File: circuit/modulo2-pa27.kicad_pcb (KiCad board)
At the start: 2 copper layers, 105 x 47 mm, 48 parts, among them J1 CONN_01X02, J3 CONN_01X04, J4 JACK_MONO, J5 HOLE, J7 HOLE, SW1 bright, U1 OPA2134, U2 OPA2134, U3 TLE2426, U4 PWR_CONN

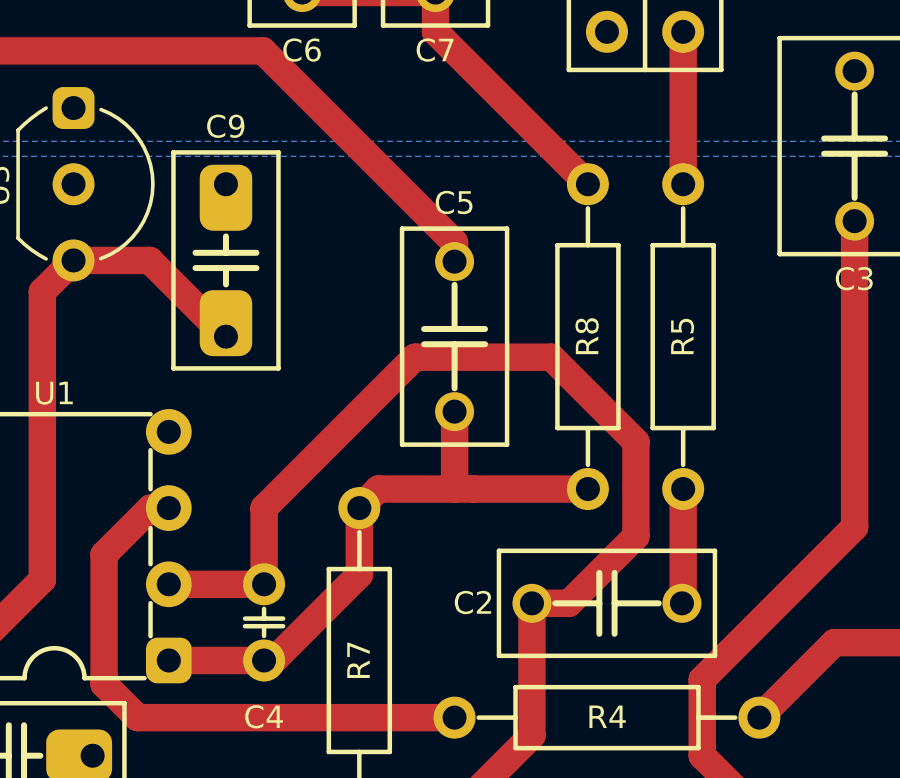
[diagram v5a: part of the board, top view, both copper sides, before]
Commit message: fixed mistakes from assembly; added bootloader; firmware changed for PCB
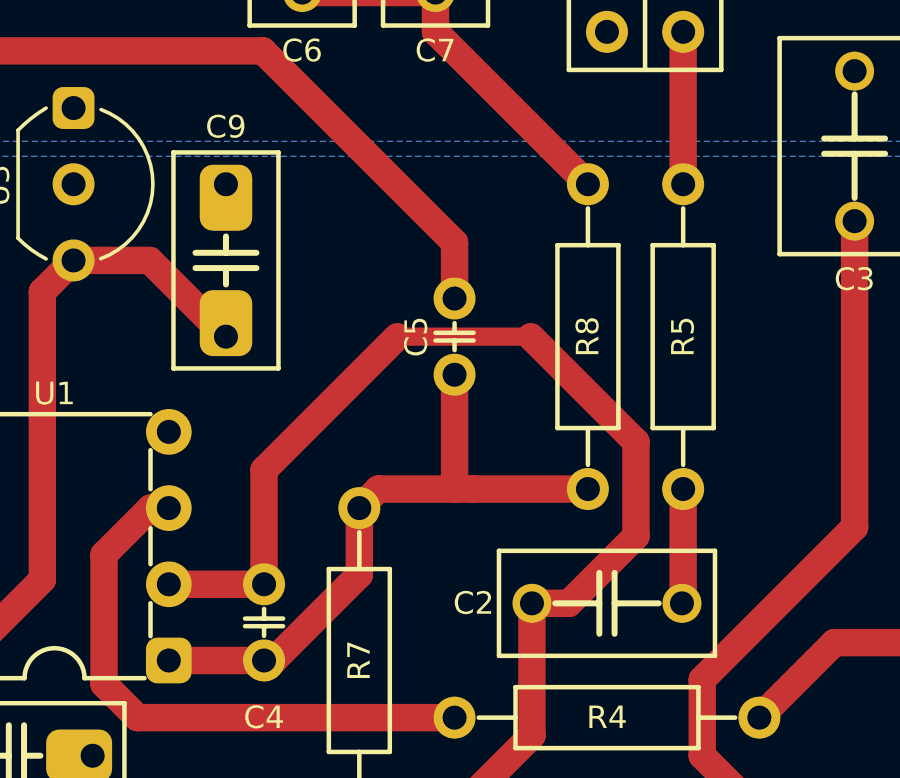
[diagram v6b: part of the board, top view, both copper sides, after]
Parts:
- C1: value 47nF -> 150nF
- C5: footprint myAmp:C_FILM_L7.2mm_W3.5mm_P5.00mm -> myAmp:C_2.5MM
- R15: value 10k -> 4k7
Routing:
- net Net-(C2-Pad2): track 40.1 -> 41.4 mm
- net Net-(C4-Pad2): track 20.2 -> 21.4 mm
- net /TRB: track 33.5 -> 34.7 mm
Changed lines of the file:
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@@
     )
   )
-  (footprint "myAmp:C_FILM_L7.2mm_W3.5mm_P5.00mm" (layer "F.Cu")
+  (footprint "myAmp:C_2.5MM" (layer "F.Cu")
     (at 107.95 72.39 90)
     (property "Sheetfile" "modulo2-pa27.kicad_sch")
     (property "Sheetname" "")
     (attr through_hole)
-    (fp_text reference "C5" (at 4.445 0) (layer "F.SilkS")
-      (effects (font (size 0.75 0.75) (thickness 0.15)))
-    )
-    (fp_text value "250pF" (at -1.016 -0.254 90) (layer "F.Fab") hide
-      (effects (font (size 0.0254 0.0254) (thickness 0.001)))
-    )
-    (fp_line (start -0.254 -1.016) (end -0.254 1.016) (layer "F.SilkS") (width 0.2))
-    (fp_line (start -3.6 -1.75) (end -3.6 1.75) (layer "F.SilkS") (width 0.15))
-    (fp_line (start -3.6 1.75) (end 3.6 1.75) (layer "F.SilkS") (width 0.15))
-    (fp_line (start 0.254 0) (end 1.725 0) (layer "F.SilkS") (width 0.2))
-    (fp_line (start 0.254 -1.016) (end 0.254 1.016) (layer "F.SilkS") (width 0.2))
-    (fp_line (start 3.6 -1.75) (end -3.6 -1.75) (layer "F.SilkS") (width 0.15))
-    (fp_line (start -0.254 0) (end -1.725 0) (layer "F.SilkS") (width 0.2))
-    (fp_line (start 3.6 1.75) (end 3.6 -1.75) (layer "F.SilkS") (width 0.15))
-    (pad "1" thru_hole circle (at -2.5 0 90) (size 1.3 1.3) (drill 0.8) (layers *.Cu *.Mask)
+    (fp_text reference "C5" (at 0 -1.27 90) (layer "F.SilkS")
+      (effects (font (size 0.75 0.75) (thickness 0.15)))
+    )
+    (fp_text value "250pF" (at -0.5715 -0.381 90) (layer "F.Fab") hide
+      (effects (font (size 0.03 0.03) (thickness 0.001)))
+    )
+    (fp_line (start -0.127 -0.635) (end -0.127 0.635) (layer "F.SilkS") (width 0.15))
+    (fp_line (start -0.127 0) (end -0.45 0) (layer "F.SilkS") (width 0.15))
+    (fp_line (start 0.127 0.635) (end 0.127 -0.635) (layer "F.SilkS") (width 0.15))
+    (fp_line (start 0.127 0) (end 0.45 0) (layer "F.SilkS") (width 0.15))
+    (pad "1" thru_hole circle (at -1.27 0 90) (size 1.4 1.4) (drill 0.8) (layers *.Cu *.Mask)
       (net 10 "Net-(C4-Pad2)") (pintype "passive"))
-    (pad "2" thru_hole circle (at 2.5 0 90) (size 1.3 1.3) (drill 0.8) (layers *.Cu *.Mask)
+    (pad "2" thru_hole circle (at 1.27 0 90) (size 1.4 1.4) (drill 0.8) (layers *.Cu *.Mask)
       (net 31 "/TRB") (pintype "passive"))
-    (model "${KIPRJMOD}/myAmp.pretty/models/C_Rect_L7.2mm_W3.5mm_P5.00mm_FKS2_FKP2_MKS2_MKP2.step"
-      (offset (xyz -2.5 0 0))
+    (model "${KIPRJMOD}/myAmp.pretty/models/C_Disc_D3.0mm_W1.6mm_P2.50mm.wrl"
+      (offset (xyz -1.25 0 0))
       (scale (xyz 1 1 1))
       (rotate (xyz 0 0 0))
@@
       (effects (font (size 0.75 0.75) (thickness 0.15)))
     )
-    (fp_text value "47nF" (at -1.016 -0.254 90) (layer "F.Fab") hide
+    (fp_text value "150nF" (at -1.016 -0.254 90) (layer "F.Fab") hide
       (effects (font (size 0.0254 0.0254) (thickness 0.001)))
     )
@@
       (effects (font (size 0.75 0.75) (thickness 0.15)))
     )
-    (fp_text value "10k" (at -2.286 0 90) (layer "F.Fab") hide
+    (fp_text value "4k7" (at -2.286 0 90) (layer "F.Fab") hide
       (effects (font (size 0.127 0.127) (thickness 0.001)))
     )
@@
   (segment (start 87 55.4) (end 87 59.695) (width 0.9144) (layer "F.Cu") (net 7))
   (segment (start 107.95 88.265) (end 110.53 85.685) (width 0.9144) (layer "F.Cu") (net 8))
+  (segment (start 101.6 80.645) (end 98.425 80.645) (width 0.9144) (layer "F.Cu") (net 8))
+  (segment (start 111.76 81.28) (end 110.53 81.28) (width 0.9144) (layer "F.Cu") (net 8))
+  (segment (start 101.6 76.835) (end 106.045 72.39) (width 0.9144) (layer "F.Cu") (net 8))
+  (segment (start 110.53 85.685) (end 110.53 81.28) (width 0.9144) (layer "F.Cu") (net 8))
+  (segment (start 101.6 80.645) (end 101.6 76.835) (width 0.9144) (layer "F.Cu") (net 8))
+  (segment (start 104.775 88.265) (end 107.95 88.265) (width 0.9144) (layer "F.Cu") (net 8))
+  (segment (start 110.49 72.39) (end 113.9952 75.8952) (width 0.9144) (layer "F.Cu") (net 8))
   (segment (start 113.9952 75.8952) (end 113.9952 79.0448) (width 0.9144) (layer "F.Cu") (net 8))
+  (segment (start 106.045 72.39) (end 110.49 72.39) (width 0.6096) (layer "F.Cu") (net 8))
   (segment (start 113.9952 79.0448) (end 111.76 81.28) (width 0.9144) (layer "F.Cu") (net 8))
-  (segment (start 101.6 80.645) (end 101.6 78.105) (width 0.9144) (layer "F.Cu") (net 8))
-  (segment (start 101.6 80.645) (end 98.425 80.645) (width 0.9144) (layer "F.Cu") (net 8))
-  (segment (start 101.6 78.105) (end 106.6292 73.0758) (width 0.9144) (layer "F.Cu") (net 8))
-  (segment (start 111.76 81.28) (end 110.53 81.28) (width 0.9144) (layer "F.Cu") (net 8))
-  (segment (start 110.53 85.685) (end 110.53 81.28) (width 0.9144) (layer "F.Cu") (net 8))
-  (segment (start 111.1758 73.0758) (end 113.9952 75.8952) (width 0.9144) (layer "F.Cu") (net 8))
-  (segment (start 106.6292 73.0758) (end 111.1758 73.0758) (width 0.9144) (layer "F.Cu") (net 8))
-  (segment (start 104.775 88.265) (end 107.95 88.265) (width 0.9144) (layer "F.Cu") (net 8))
   (segment (start 116.205 86.36) (end 116.205 83.82) (width 0.9144) (layer "F.Cu") (net 9))
   (segment (start 121.285 78.74) (end 121.285 68.54) (width 0.9144) (layer "F.Cu") (net 9))
@@
   (segment (start 108.585 77.47) (end 105.41 77.47) (width 0.9144) (layer "F.Cu") (net 10))
   (segment (start 112.395 77.47) (end 108.585 77.47) (width 0.9144) (layer "F.Cu") (net 10))
-  (segment (start 107.95 74.89) (end 107.95 77.47) (width 0.9144) (layer "F.Cu") (net 10))
   (segment (start 104.775 80.3275) (end 104.775 78.105) (width 0.9144) (layer "F.Cu") (net 10))
   (segment (start 98.425 83.185) (end 101.6 83.185) (width 0.9144) (layer "F.Cu") (net 10))
   (segment (start 101.6 83.185) (end 101.9175 83.185) (width 0.9144) (layer "F.Cu") (net 10))
+  (segment (start 107.95 73.66) (end 107.95 77.47) (width 0.9144) (layer "F.Cu") (net 10))
   (segment (start 101.9175 83.185) (end 104.775 80.3275) (width 0.9144) (layer "F.Cu") (net 10))
   (segment (start 105.41 77.47) (end 104.775 78.105) (width 0.9144) (layer "F.Cu") (net 10))
@@
   (segment (start 69.215 62.23) (end 69.215 73.66) (width 0.9144) (layer "F.Cu") (net 29))
   (segment (start 115.57 67.31) (end 115.57 62.23) (width 0.9144) (layer "F.Cu") (net 30))
-  (segment (start 107.95 69.89) (end 107.95 69.255) (width 0.9144) (layer "F.Cu") (net 31))
   (segment (start 85.725 62.865) (end 84.5 61.64) (width 0.9144) (layer "F.Cu") (net 31))
+  (segment (start 107.95 69.255) (end 101.56 62.865) (width 0.9144) (layer "F.Cu") (net 31))
+  (segment (start 107.95 71.12) (end 107.95 69.255) (width 0.9144) (layer "F.Cu") (net 31))
   (segment (start 84.5 61.64) (end 84.5 55.4) (width 0.9144) (layer "F.Cu") (net 31))
-  (segment (start 107.95 69.255) (end 101.56 62.865) (width 0.9144) (layer "F.Cu") (net 31))
   (segment (start 101.56 62.865) (end 85.725 62.865) (width 0.9144) (layer "F.Cu") (net 31))
   (segment (start 121.285 53.34) (end 123.345 55.4) (width 0.9144) (layer "F.Cu") (net 32))

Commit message: reduced preamp gain to not clip the FV-1; timer_ticks_high();
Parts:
- R15: value 4k7 -> 2k2
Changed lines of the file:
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@@
     )
     (fp_line (start -0.127 -0.635) (end -0.127 0.635) (layer "F.SilkS") (width 0.15))
+    (fp_line (start 0.127 0.635) (end 0.127 -0.635) (layer "F.SilkS") (width 0.15))
     (fp_line (start -0.127 0) (end -0.45 0) (layer "F.SilkS") (width 0.15))
-    (fp_line (start 0.127 0.635) (end 0.127 -0.635) (layer "F.SilkS") (width 0.15))
     (fp_line (start 0.127 0) (end 0.45 0) (layer "F.SilkS") (width 0.15))
     (pad "1" thru_hole circle (at -1.27 0 90) (size 1.4 1.4) (drill 0.8) (layers *.Cu *.Mask)
@@
       (effects (font (size 0.75 0.75) (thickness 0.15)))
     )
-    (fp_text value "4k7" (at -2.286 0 90) (layer "F.Fab") hide
+    (fp_text value "2k2" (at -2.286 0 90) (layer "F.Fab") hide
       (effects (font (size 0.127 0.127) (thickness 0.001)))
     )
     (fp_line (start 3.048 -1.016) (end 3.048 1.016) (layer "F.SilkS") (width 0.15))
+    (fp_line (start 3.048 0) (end 4.275 0) (layer "F.SilkS") (width 0.15))
     (fp_line (start -3.048 0) (end -4.275 0) (layer "F.SilkS") (width 0.15))
     (fp_line (start -3.048 -1.016) (end -3.048 1.016) (layer "F.SilkS") (width 0.15))
-    (fp_line (start 3.048 0) (end 4.275 0) (layer "F.SilkS") (width 0.15))
     (fp_line (start -3.048 -1.016) (end 3.048 -1.016) (layer "F.SilkS") (width 0.15))
     (fp_line (start -3.048 1.016) (end 3.048 1.016) (layer "F.SilkS") (width 0.15))
